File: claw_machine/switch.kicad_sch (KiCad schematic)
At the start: 4 parts, among them J801 Conn_01x02, J802 Screw_Terminal_01x02, SW4 SW_Push

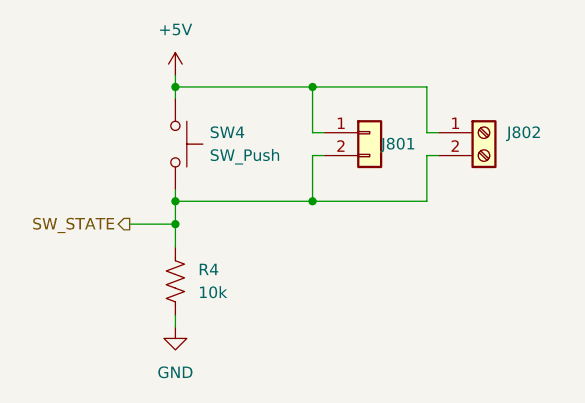
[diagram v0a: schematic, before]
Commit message: Assign footprints
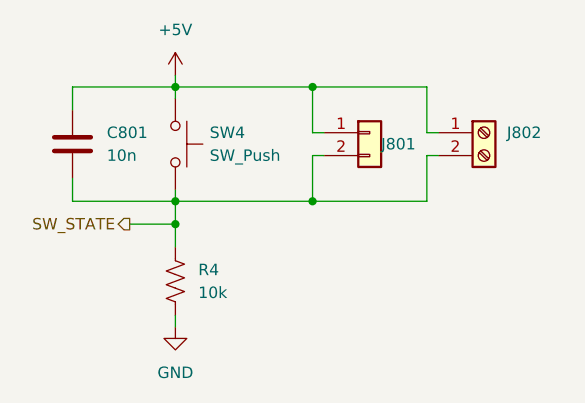
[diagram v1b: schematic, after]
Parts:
- added C801: 10n, Capacitor_SMD:C_1206_3216Metric_Pad1.33x1.80mm_HandSolder, symbol Device:C
- J801: footprint (none) -> Connector_PinHeader_2.54mm:PinHeader_1x02_P2.54mm_Vertical
- R4: footprint Resistor_SMD:R_0805_2012Metric_Pad1.20x1.40mm_HandSolder -> Resistor_SMD:R_1206_3216Metric_Pad1.30x1.75mm_HandSolder
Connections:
- net +5V: now also C801.1
- net SW_STATE: now also C801.2
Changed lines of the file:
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@@
+    (stroke (width 0) (type default))
+  )
+  (wire (pts (xy 63.5 60.96) (xy 74.93 60.96))
+    (stroke (width 0) (type default))
+  )
+  (wire (pts (xy 63.5 48.26) (xy 74.93 48.26))
     (stroke (width 0) (type default))
   )
@@
     (stroke (width 0) (type default))
   )
+  (wire (pts (xy 63.5 58.42) (xy 63.5 60.96))
+    (stroke (width 0) (type default))
+  )
   (wire (pts (xy 74.93 63.5) (xy 74.93 66.04))
     (stroke (width 0) (type default))
@@
   )
   (wire (pts (xy 74.93 46.99) (xy 74.93 48.26))
+    (stroke (width 0) (type default))
+  )
+  (wire (pts (xy 63.5 50.8) (xy 63.5 48.26))
     (stroke (width 0) (type default))
   )
@@
   (hierarchical_label "SW_STATE" (shape output) (at 69.85 63.5 180) (fields_autoplaced)
     (effects (font (size 1.27 1.27)) (justify right))
+  )
+  (symbol (lib_id "Device:C") (at 63.5 54.61 0) (mirror y) (unit 1)
+    (in_bom yes) (on_board yes) (dnp no) (fields_autoplaced)
+    (property "Reference" "C801" (at 67.31 53.34 0)
+      (effects (font (size 1.27 1.27)) (justify right))
+    )
+    (property "Value" "10n" (at 67.31 55.88 0)
+      (effects (font (size 1.27 1.27)) (justify right))
+    )
+    (property "Footprint" "Capacitor_SMD:C_1206_3216Metric_Pad1.33x1.80mm_HandSolder" (at 62.5348 58.42 0)
+      (effects (font (size 1.27 1.27)) hide)
+    )
+    (property "Datasheet" "~" (at 63.5 54.61 0)
+      (effects (font (size 1.27 1.27)) hide)
+    )
+    (pin "1")
+    (pin "2")
+    (instances
+      (project "claw_machine"
+        (path "/2e48e9a4-e55f-4bd7-8086-6a8b9c5eabc1/9c0456e1-be0f-4687-848b-2e8f026580ef"
+          (reference "C801") (unit 1)
+        )
+        (path "/2e48e9a4-e55f-4bd7-8086-6a8b9c5eabc1/faf0a1bb-bf1c-4d47-bb23-2823bfc2f254"
+          (reference "C901") (unit 1)
+        )
+        (path "/2e48e9a4-e55f-4bd7-8086-6a8b9c5eabc1/b1544965-a031-4321-9ea3-4ec80e6ff7b9"
+          (reference "C1001") (unit 1)
+        )
+        (path "/2e48e9a4-e55f-4bd7-8086-6a8b9c5eabc1/5cef106b-2aca-4cae-bdf2-e4f8176850ad"
+          (reference "C1101") (unit 1)
+        )
+        (path "/2e48e9a4-e55f-4bd7-8086-6a8b9c5eabc1/fe5502bf-d68b-4deb-962c-eedd145df63d"
+          (reference "C1201") (unit 1)
+        )
+        (path "/2e48e9a4-e55f-4bd7-8086-6a8b9c5eabc1/e3607caa-def2-4de9-9283-b41712be4e57"
+          (reference "C1301") (unit 1)
+        )
+        (path "/2e48e9a4-e55f-4bd7-8086-6a8b9c5eabc1/3a275a35-ac75-436b-ba62-b5574177f89b"
+          (reference "C1401") (unit 1)
+        )
+        (path "/2e48e9a4-e55f-4bd7-8086-6a8b9c5eabc1/711d7158-7287-4132-8369-831ffc2ac021"
+          (reference "C1501") (unit 1)
+        )
+      )
+    )
   )
   (symbol (lib_id "power:+5V") (at 74.93 46.99 0) (unit 1)
@@
       (effects (font (size 1.27 1.27)) (justify right))
     )
-    (property "Footprint" "Resistor_SMD:R_0805_2012Metric_Pad1.20x1.40mm_HandSolder" (at 73.914 69.596 90)
+    (property "Footprint" "Resistor_SMD:R_1206_3216Metric_Pad1.30x1.75mm_HandSolder" (at 73.914 69.596 90)
       (effects (font (size 1.27 1.27)) hide)
     )
@@
       (effects (font (size 1.27 1.27)) (justify left) hide)
     )
-    (property "Footprint" "" (at 96.52 53.34 0)
-      (effects (font (size 1.27 1.27)) hide)
-    )
+    (property "Footprint" "Connector_PinHeader_2.54mm:PinHeader_1x02_P2.54mm_Vertical" (at 96.52 53.34 0)
+      (effects (font (size 1.27 1.27)) hide)
+    )

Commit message: Tiny bit of PCB work
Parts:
- removed R4: 10k, Resistor_SMD:R_1206_3216Metric_Pad1.30x1.75mm_HandSolder, symbol Device:R_US
- added R105: 10k, Resistor_SMD:R_1206_3216Metric_Pad1.30x1.75mm_HandSolder, symbol Device:R
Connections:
- net GND: now also R105.2
- net SW_STATE: now also R105.1
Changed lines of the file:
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@@
 (kicad_sch (version 20230121) (generator eeschema)
   (paper "A5")
+  (junction (at 74.93 62.23) (diameter 0) (color 0 0 0 0)
+  )
   (junction (at 74.93 48.26) (diameter 0) (color 0 0 0 0)
   )
   (junction (at 90.17 60.96) (diameter 0) (color 0 0 0 0)
   )
-  (junction (at 74.93 63.5) (diameter 0) (color 0 0 0 0)
+  (junction (at 74.93 64.77) (diameter 0) (color 0 0 0 0)
   )
   (junction (at 74.93 60.96) (diameter 0) (color 0 0 0 0)
@@
     (stroke (width 0) (type default))
   )
+  (wire (pts (xy 74.93 62.23) (xy 74.93 60.96))
+    (stroke (width 0) (type default))
+  )
   (wire (pts (xy 102.87 48.26) (xy 90.17 48.26))
     (stroke (width 0) (type default))
@@
     (stroke (width 0) (type default))
   )
-  (wire (pts (xy 63.5 60.96) (xy 74.93 60.96))
+  (wire (pts (xy 63.5 62.23) (xy 74.93 62.23))
     (stroke (width 0) (type default))
   )
@@
     (stroke (width 0) (type default))
   )
+  (wire (pts (xy 74.93 64.77) (xy 74.93 66.04))
+    (stroke (width 0) (type default))
+  )
   (wire (pts (xy 102.87 53.34) (xy 104.14 53.34))
     (stroke (width 0) (type default))
@@
     (stroke (width 0) (type default))
   )
-  (wire (pts (xy 69.85 63.5) (xy 74.93 63.5))
+  (wire (pts (xy 69.85 64.77) (xy 74.93 64.77))
     (stroke (width 0) (type default))
   )
@@
     (stroke (width 0) (type default))
   )
-  (wire (pts (xy 63.5 58.42) (xy 63.5 60.96))
-    (stroke (width 0) (type default))
-  )
-  (wire (pts (xy 74.93 63.5) (xy 74.93 66.04))
-    (stroke (width 0) (type default))
-  )
-  (wire (pts (xy 74.93 60.96) (xy 74.93 63.5))
+  (wire (pts (xy 63.5 58.42) (xy 63.5 62.23))
+    (stroke (width 0) (type default))
+  )
+  (wire (pts (xy 74.93 62.23) (xy 74.93 64.77))
     (stroke (width 0) (type default))
   )
@@
     (stroke (width 0) (type default))
   )
-  (hierarchical_label "SW_STATE" (shape output) (at 69.85 63.5 180) (fields_autoplaced)
+  (hierarchical_label "SW_STATE" (shape output) (at 69.85 64.77 180) (fields_autoplaced)
     (effects (font (size 1.27 1.27)) (justify right))
   )
@@
     )
   )
-  (symbol (lib_id "Device:R_US") (at 74.93 69.85 180) (unit 1)
-    (in_bom yes) (on_board yes) (dnp no) (fields_autoplaced)
-    (property "Reference" "R4" (at 77.47 68.58 0)
-      (effects (font (size 1.27 1.27)) (justify right))
-    )
-    (property "Value" "10k" (at 77.47 71.12 0)
-      (effects (font (size 1.27 1.27)) (justify right))
-    )
-    (property "Footprint" "Resistor_SMD:R_1206_3216Metric_Pad1.30x1.75mm_HandSolder" (at 73.914 69.596 90)
-      (effects (font (size 1.27 1.27)) hide)
-    )
-    (property "Datasheet" "~" (at 74.93 69.85 0)
-      (effects (font (size 1.27 1.27)) hide)
-    )
-    (pin "1")
-    (pin "2")
-    (instances
-      (project "claw_machine"
-        (path "/2e48e9a4-e55f-4bd7-8086-6a8b9c5eabc1/6818ac2a-ce5d-423a-9389-7753b58c3ff7"
-          (reference "R4") (unit 1)
-        )
-        (path "/2e48e9a4-e55f-4bd7-8086-6a8b9c5eabc1/9c0456e1-be0f-4687-848b-2e8f026580ef"
-          (reference "R801") (unit 1)
-        )
-        (path "/2e48e9a4-e55f-4bd7-8086-6a8b9c5eabc1/faf0a1bb-bf1c-4d47-bb23-2823bfc2f254"
-          (reference "R901") (unit 1)
-        )
-        (path "/2e48e9a4-e55f-4bd7-8086-6a8b9c5eabc1/b1544965-a031-4321-9ea3-4ec80e6ff7b9"
-          (reference "R1001") (unit 1)
-        )
-        (path "/2e48e9a4-e55f-4bd7-8086-6a8b9c5eabc1/5cef106b-2aca-4cae-bdf2-e4f8176850ad"
-          (reference "R1101") (unit 1)
-        )
-        (path "/2e48e9a4-e55f-4bd7-8086-6a8b9c5eabc1/fe5502bf-d68b-4deb-962c-eedd145df63d"
-          (reference "R1201") (unit 1)
-        )
-        (path "/2e48e9a4-e55f-4bd7-8086-6a8b9c5eabc1/e3607caa-def2-4de9-9283-b41712be4e57"
-          (reference "R1301") (unit 1)
-        )
-        (path "/2e48e9a4-e55f-4bd7-8086-6a8b9c5eabc1/3a275a35-ac75-436b-ba62-b5574177f89b"
-          (reference "R1401") (unit 1)
-        )
-        (path "/2e48e9a4-e55f-4bd7-8086-6a8b9c5eabc1/711d7158-7287-4132-8369-831ffc2ac021"
-          (reference "R1501") (unit 1)
-        )
-      )
-      (project "ClawMachine"
-        (path "/aafe1d38-cfbd-4a85-a256-fbe14cd8b9f5"
-          (reference "R19") (unit 1)
-        )
-        (path "/aafe1d38-cfbd-4a85-a256-fbe14cd8b9f5/023b6910-a968-479e-88ee-414e77016c63/647f2669-19ce-476d-b63f-0ff9b7f86926"
-          (reference "R23") (unit 1)
-        )
-        (path "/aafe1d38-cfbd-4a85-a256-fbe14cd8b9f5/023b6910-a968-479e-88ee-414e77016c63/2b5a80b9-bc44-4eb9-a82c-2f335e668733"
-          (reference "R24") (unit 1)
-        )
-        (path "/aafe1d38-cfbd-4a85-a256-fbe14cd8b9f5/023b6910-a968-479e-88ee-414e77016c63/827f60d8-73fb-49af-ad66-d3e0d4953281"
-          (reference "R22") (unit 1)
-        )
-        (path "/aafe1d38-cfbd-4a85-a256-fbe14cd8b9f5/023b6910-a968-479e-88ee-414e77016c63/3454ba60-c9bc-4dd4-b51a-e52c59c8870c"
-          (reference "R21") (unit 1)
-        )
-        (path "/aafe1d38-cfbd-4a85-a256-fbe14cd8b9f5/023b6910-a968-479e-88ee-414e77016c63/d1a37237-ebf6-4b13-b22e-f466e93cd233"
-          (reference "R25") (unit 1)
-        )
-      )
-    )
-  )
   (symbol (lib_id "Connector:Screw_Terminal_01x02") (at 109.22 53.34 0) (unit 1)
     (in_bom yes) (on_board yes) (dnp no) (fields_autoplaced)
@@
         )
       )
+    )
+  )
+  (symbol (lib_id "Device:R") (at 74.93 69.85 0) (unit 1)
+    (in_bom yes) (on_board yes) (dnp no) (fields_autoplaced)
+    (property "Reference" "R105" (at 77.47 68.58 0)
+      (effects (font (size 1.27 1.27)) (justify left))
+    )
+    (property "Value" "10k" (at 77.47 71.12 0)
+      (effects (font (size 1.27 1.27)) (justify left))
+    )
+    (property "Footprint" "Resistor_SMD:R_1206_3216Metric_Pad1.30x1.75mm_HandSolder" (at 73.152 69.85 90)
+      (effects (font (size 1.27 1.27)) hide)
+    )
+    (property "Datasheet" "~" (at 74.93 69.85 0)
+      (effects (font (size 1.27 1.27)) hide)
+    )
+    (pin "1")
+    (pin "2")
+    (instances
+      (project "claw_machine"
+        (path "/2e48e9a4-e55f-4bd7-8086-6a8b9c5eabc1"
+          (reference "R105") (unit 1)
+        )
+        (path "/2e48e9a4-e55f-4bd7-8086-6a8b9c5eabc1/9c0456e1-be0f-4687-848b-2e8f026580ef"
+          (reference "R801") (unit 1)
+        )
+        (path "/2e48e9a4-e55f-4bd7-8086-6a8b9c5eabc1/faf0a1bb-bf1c-4d47-bb23-2823bfc2f254"
+          (reference "R901") (unit 1)
+        )
+        (path "/2e48e9a4-e55f-4bd7-8086-6a8b9c5eabc1/b1544965-a031-4321-9ea3-4ec80e6ff7b9"
+          (reference "R1001") (unit 1)
+        )
+        (path "/2e48e9a4-e55f-4bd7-8086-6a8b9c5eabc1/5cef106b-2aca-4cae-bdf2-e4f8176850ad"
+          (reference "R1101") (unit 1)
+        )
+        (path "/2e48e9a4-e55f-4bd7-8086-6a8b9c5eabc1/fe5502bf-d68b-4deb-962c-eedd145df63d"
+          (reference "R1201") (unit 1)
+        )
+        (path "/2e48e9a4-e55f-4bd7-8086-6a8b9c5eabc1/e3607caa-def2-4de9-9283-b41712be4e57"
+          (reference "R1301") (unit 1)
+        )
+        (path "/2e48e9a4-e55f-4bd7-8086-6a8b9c5eabc1/3a275a35-ac75-436b-ba62-b5574177f89b"
+          (reference "R1401") (unit 1)
+        )
+        (path "/2e48e9a4-e55f-4bd7-8086-6a8b9c5eabc1/711d7158-7287-4132-8369-831ffc2ac021"
+          (reference "R1501") (unit 1)
+        )
+      )

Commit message: Do most of the PCB layout
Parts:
- renumbered J802 to J1502
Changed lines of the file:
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@@
   (symbol (lib_id "Connector:Screw_Terminal_01x02") (at 109.22 53.34 0) (unit 1)
     (in_bom yes) (on_board yes) (dnp no) (fields_autoplaced)
-    (property "Reference" "J802" (at 111.76 53.34 0)
+    (property "Reference" "J1502" (at 111.76 53.34 0)
       (effects (font (size 1.27 1.27)) (justify left))
     )
@@
     (instances
       (project "claw_machine"
+        (path "/2e48e9a4-e55f-4bd7-8086-6a8b9c5eabc1/711d7158-7287-4132-8369-831ffc2ac021"
+          (reference "J1502") (unit 1)
+        )
         (path "/2e48e9a4-e55f-4bd7-8086-6a8b9c5eabc1/9c0456e1-be0f-4687-848b-2e8f026580ef"
           (reference "J802") (unit 1)
@@
           (reference "J1402") (unit 1)
         )
-        (path "/2e48e9a4-e55f-4bd7-8086-6a8b9c5eabc1/711d7158-7287-4132-8369-831ffc2ac021"
-          (reference "J1502") (unit 1)
-        )
       )
       (project "ClawMachine"
-        (path "/aafe1d38-cfbd-4a85-a256-fbe14cd8b9f5"
-          (reference "J10") (unit 1)
+        (path "/aafe1d38-cfbd-4a85-a256-fbe14cd8b9f5/66d7bc32-fbc5-464c-b216-02a1923ceee2/08f65624-f4fa-418f-9d18-6be89430fb3d"
+          (reference "J52") (unit 1)
+        )
+        (path "/aafe1d38-cfbd-4a85-a256-fbe14cd8b9f5/66d7bc32-fbc5-464c-b216-02a1923ceee2/9f3309e4-ab13-4543-82c5-3314fad4fb42"
+          (reference "J28") (unit 1)
+        )
+        (path "/aafe1d38-cfbd-4a85-a256-fbe14cd8b9f5/66d7bc32-fbc5-464c-b216-02a1923ceee2/c840e683-8e5c-4244-aa04-aa550b475b61"
+          (reference "J30") (unit 1)
+        )
+        (path "/aafe1d38-cfbd-4a85-a256-fbe14cd8b9f5/66d7bc32-fbc5-464c-b216-02a1923ceee2/cb237415-f5e3-4ab8-8a18-bb0c712cf170"
+          (reference "J37") (unit 1)
+        )
+        (path "/aafe1d38-cfbd-4a85-a256-fbe14cd8b9f5/66d7bc32-fbc5-464c-b216-02a1923ceee2/19f6ccc4-ee86-4d04-b387-d16ba462ba1d"
+          (reference "J32") (unit 1)
+        )
+        (path "/aafe1d38-cfbd-4a85-a256-fbe14cd8b9f5/66d7bc32-fbc5-464c-b216-02a1923ceee2/9dcc0cd6-b0a2-46e3-bd19-3d60078b727b"
+          (reference "J44") (unit 1)
+        )
+        (path "/aafe1d38-cfbd-4a85-a256-fbe14cd8b9f5/66d7bc32-fbc5-464c-b216-02a1923ceee2/908044b4-57ba-4dbb-884f-6721522819f5"
+          (reference "J46") (unit 1)
+        )
+        (path "/aafe1d38-cfbd-4a85-a256-fbe14cd8b9f5/66d7bc32-fbc5-464c-b216-02a1923ceee2/7b210caa-f29c-48de-9463-8c7367b047b2"
+          (reference "J50") (unit 1)
+        )
+        (path "/aafe1d38-cfbd-4a85-a256-fbe14cd8b9f5/66d7bc32-fbc5-464c-b216-02a1923ceee2/754a2901-ff53-43bc-aab2-65886d773990"
+          (reference "J48") (unit 1)
         )
         (path "/aafe1d38-cfbd-4a85-a256-fbe14cd8b9f5/66d7bc32-fbc5-464c-b216-02a1923ceee2/b9e60182-978d-4bd3-aec0-6053504def0e"
           (reference "J54") (unit 1)
         )
-        (path "/aafe1d38-cfbd-4a85-a256-fbe14cd8b9f5/66d7bc32-fbc5-464c-b216-02a1923ceee2/754a2901-ff53-43bc-aab2-65886d773990"
-          (reference "J48") (unit 1)
-        )
-        (path "/aafe1d38-cfbd-4a85-a256-fbe14cd8b9f5/66d7bc32-fbc5-464c-b216-02a1923ceee2/7b210caa-f29c-48de-9463-8c7367b047b2"
-          (reference "J50") (unit 1)
-        )
-        (path "/aafe1d38-cfbd-4a85-a256-fbe14cd8b9f5/66d7bc32-fbc5-464c-b216-02a1923ceee2/908044b4-57ba-4dbb-884f-6721522819f5"
-          (reference "J46") (unit 1)
-        )
-        (path "/aafe1d38-cfbd-4a85-a256-fbe14cd8b9f5/66d7bc32-fbc5-464c-b216-02a1923ceee2/9dcc0cd6-b0a2-46e3-bd19-3d60078b727b"
-          (reference "J44") (unit 1)
-        )
-        (path "/aafe1d38-cfbd-4a85-a256-fbe14cd8b9f5/66d7bc32-fbc5-464c-b216-02a1923ceee2/19f6ccc4-ee86-4d04-b387-d16ba462ba1d"
-          (reference "J32") (unit 1)
-        )
-        (path "/aafe1d38-cfbd-4a85-a256-fbe14cd8b9f5/66d7bc32-fbc5-464c-b216-02a1923ceee2/cb237415-f5e3-4ab8-8a18-bb0c712cf170"
-          (reference "J37") (unit 1)
-        )
-        (path "/aafe1d38-cfbd-4a85-a256-fbe14cd8b9f5/66d7bc32-fbc5-464c-b216-02a1923ceee2/c840e683-8e5c-4244-aa04-aa550b475b61"
-          (reference "J30") (unit 1)
-        )
-        (path "/aafe1d38-cfbd-4a85-a256-fbe14cd8b9f5/66d7bc32-fbc5-464c-b216-02a1923ceee2/9f3309e4-ab13-4543-82c5-3314fad4fb42"
-          (reference "J28") (unit 1)
-        )
-        (path "/aafe1d38-cfbd-4a85-a256-fbe14cd8b9f5/66d7bc32-fbc5-464c-b216-02a1923ceee2/08f65624-f4fa-418f-9d18-6be89430fb3d"
-          (reference "J52") (unit 1)
+        (path "/aafe1d38-cfbd-4a85-a256-fbe14cd8b9f5"
+          (reference "J10") (unit 1)
         )
       )

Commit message: Route all power traced and replicated sections
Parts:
- renumbered J1502 to J902
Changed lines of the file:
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@@
   (symbol (lib_id "Connector:Screw_Terminal_01x02") (at 109.22 53.34 0) (unit 1)
     (in_bom yes) (on_board yes) (dnp no) (fields_autoplaced)
-    (property "Reference" "J1502" (at 111.76 53.34 0)
+    (property "Reference" "J902" (at 111.76 53.34 0)
       (effects (font (size 1.27 1.27)) (justify left))
     )
@@
     (instances
       (project "claw_machine"
-        (path "/2e48e9a4-e55f-4bd7-8086-6a8b9c5eabc1/711d7158-7287-4132-8369-831ffc2ac021"
-          (reference "J1502") (unit 1)
-        )
-        (path "/2e48e9a4-e55f-4bd7-8086-6a8b9c5eabc1/9c0456e1-be0f-4687-848b-2e8f026580ef"
-          (reference "J802") (unit 1)
-        )
         (path "/2e48e9a4-e55f-4bd7-8086-6a8b9c5eabc1/faf0a1bb-bf1c-4d47-bb23-2823bfc2f254"
           (reference "J902") (unit 1)
@@
           (reference "J1402") (unit 1)
         )
+        (path "/2e48e9a4-e55f-4bd7-8086-6a8b9c5eabc1/711d7158-7287-4132-8369-831ffc2ac021"
+          (reference "J1502") (unit 1)
+        )
+        (path "/2e48e9a4-e55f-4bd7-8086-6a8b9c5eabc1/9c0456e1-be0f-4687-848b-2e8f026580ef"
+          (reference "J802") (unit 1)
+        )
       )

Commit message: Minor change reconcile
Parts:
- renumbered J902 to J1002
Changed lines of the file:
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@@
   (symbol (lib_id "Connector:Screw_Terminal_01x02") (at 109.22 53.34 0) (unit 1)
     (in_bom yes) (on_board yes) (dnp no) (fields_autoplaced)
-    (property "Reference" "J902" (at 111.76 53.34 0)
+    (property "Reference" "J1002" (at 111.76 53.34 0)
       (effects (font (size 1.27 1.27)) (justify left))
     )
@@
     (instances
       (project "claw_machine"
-        (path "/2e48e9a4-e55f-4bd7-8086-6a8b9c5eabc1/faf0a1bb-bf1c-4d47-bb23-2823bfc2f254"
-          (reference "J902") (unit 1)
-        )
         (path "/2e48e9a4-e55f-4bd7-8086-6a8b9c5eabc1/b1544965-a031-4321-9ea3-4ec80e6ff7b9"
           (reference "J1002") (unit 1)
@@
           (reference "J802") (unit 1)
         )
+        (path "/2e48e9a4-e55f-4bd7-8086-6a8b9c5eabc1/faf0a1bb-bf1c-4d47-bb23-2823bfc2f254"
+          (reference "J902") (unit 1)
+        )
       )
       (project "ClawMachine"
-        (path "/aafe1d38-cfbd-4a85-a256-fbe14cd8b9f5/66d7bc32-fbc5-464c-b216-02a1923ceee2/08f65624-f4fa-418f-9d18-6be89430fb3d"
-          (reference "J52") (unit 1)
+        (path "/aafe1d38-cfbd-4a85-a256-fbe14cd8b9f5"
+          (reference "J10") (unit 1)
+        )
+        (path "/aafe1d38-cfbd-4a85-a256-fbe14cd8b9f5/66d7bc32-fbc5-464c-b216-02a1923ceee2/b9e60182-978d-4bd3-aec0-6053504def0e"
+          (reference "J54") (unit 1)
+        )
+        (path "/aafe1d38-cfbd-4a85-a256-fbe14cd8b9f5/66d7bc32-fbc5-464c-b216-02a1923ceee2/754a2901-ff53-43bc-aab2-65886d773990"
+          (reference "J48") (unit 1)
+        )
+        (path "/aafe1d38-cfbd-4a85-a256-fbe14cd8b9f5/66d7bc32-fbc5-464c-b216-02a1923ceee2/7b210caa-f29c-48de-9463-8c7367b047b2"
+          (reference "J50") (unit 1)
+        )
+        (path "/aafe1d38-cfbd-4a85-a256-fbe14cd8b9f5/66d7bc32-fbc5-464c-b216-02a1923ceee2/908044b4-57ba-4dbb-884f-6721522819f5"
+          (reference "J46") (unit 1)
+        )
+        (path "/aafe1d38-cfbd-4a85-a256-fbe14cd8b9f5/66d7bc32-fbc5-464c-b216-02a1923ceee2/9dcc0cd6-b0a2-46e3-bd19-3d60078b727b"
+          (reference "J44") (unit 1)
+        )
+        (path "/aafe1d38-cfbd-4a85-a256-fbe14cd8b9f5/66d7bc32-fbc5-464c-b216-02a1923ceee2/19f6ccc4-ee86-4d04-b387-d16ba462ba1d"
+          (reference "J32") (unit 1)
+        )
+        (path "/aafe1d38-cfbd-4a85-a256-fbe14cd8b9f5/66d7bc32-fbc5-464c-b216-02a1923ceee2/cb237415-f5e3-4ab8-8a18-bb0c712cf170"
+          (reference "J37") (unit 1)
+        )
+        (path "/aafe1d38-cfbd-4a85-a256-fbe14cd8b9f5/66d7bc32-fbc5-464c-b216-02a1923ceee2/c840e683-8e5c-4244-aa04-aa550b475b61"
+          (reference "J30") (unit 1)
         )
         (path "/aafe1d38-cfbd-4a85-a256-fbe14cd8b9f5/66d7bc32-fbc5-464c-b216-02a1923ceee2/9f3309e4-ab13-4543-82c5-3314fad4fb42"
           (reference "J28") (unit 1)
         )
-        (path "/aafe1d38-cfbd-4a85-a256-fbe14cd8b9f5/66d7bc32-fbc5-464c-b216-02a1923ceee2/c840e683-8e5c-4244-aa04-aa550b475b61"
-          (reference "J30") (unit 1)
-        )
-        (path "/aafe1d38-cfbd-4a85-a256-fbe14cd8b9f5/66d7bc32-fbc5-464c-b216-02a1923ceee2/cb237415-f5e3-4ab8-8a18-bb0c712cf170"
-          (reference "J37") (unit 1)
-        )
-        (path "/aafe1d38-cfbd-4a85-a256-fbe14cd8b9f5/66d7bc32-fbc5-464c-b216-02a1923ceee2/19f6ccc4-ee86-4d04-b387-d16ba462ba1d"
-          (reference "J32") (unit 1)
-        )
-        (path "/aafe1d38-cfbd-4a85-a256-fbe14cd8b9f5/66d7bc32-fbc5-464c-b216-02a1923ceee2/9dcc0cd6-b0a2-46e3-bd19-3d60078b727b"
-          (reference "J44") (unit 1)
-        )
-        (path "/aafe1d38-cfbd-4a85-a256-fbe14cd8b9f5/66d7bc32-fbc5-464c-b216-02a1923ceee2/908044b4-57ba-4dbb-884f-6721522819f5"
-          (reference "J46") (unit 1)
-        )
-        (path "/aafe1d38-cfbd-4a85-a256-fbe14cd8b9f5/66d7bc32-fbc5-464c-b216-02a1923ceee2/7b210caa-f29c-48de-9463-8c7367b047b2"
-          (reference "J50") (unit 1)
-        )
-        (path "/aafe1d38-cfbd-4a85-a256-fbe14cd8b9f5/66d7bc32-fbc5-464c-b216-02a1923ceee2/754a2901-ff53-43bc-aab2-65886d773990"
-          (reference "J48") (unit 1)
-        )
-        (path "/aafe1d38-cfbd-4a85-a256-fbe14cd8b9f5/66d7bc32-fbc5-464c-b216-02a1923ceee2/b9e60182-978d-4bd3-aec0-6053504def0e"
-          (reference "J54") (unit 1)
-        )
-        (path "/aafe1d38-cfbd-4a85-a256-fbe14cd8b9f5"
-          (reference "J10") (unit 1)
+        (path "/aafe1d38-cfbd-4a85-a256-fbe14cd8b9f5/66d7bc32-fbc5-464c-b216-02a1923ceee2/08f65624-f4fa-418f-9d18-6be89430fb3d"
+          (reference "J52") (unit 1)
         )
       )
